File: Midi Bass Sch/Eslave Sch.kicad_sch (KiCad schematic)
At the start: 16 parts, among them M1 Stepper_Motor_bipolar, Q9 BDW93C, SW1 SW_Push, U2 PIC16F1788, U4 TMC2209

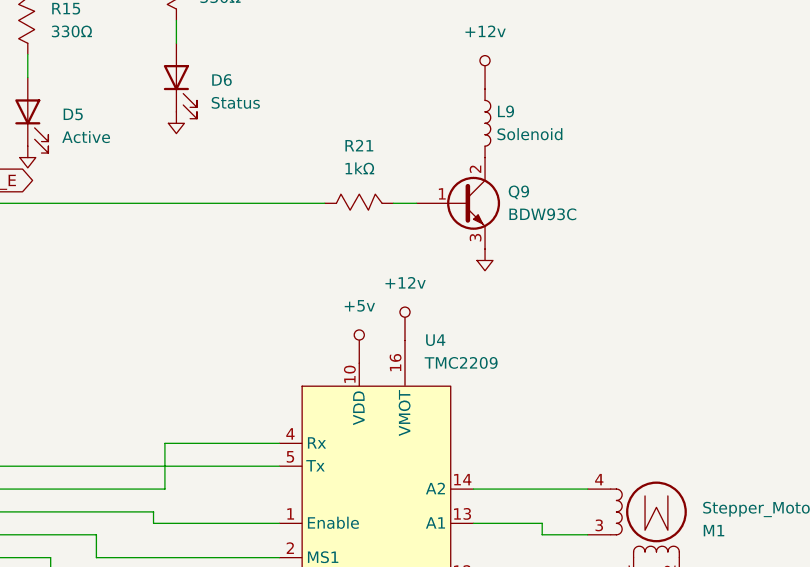
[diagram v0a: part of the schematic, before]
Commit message: updated stepper voltage
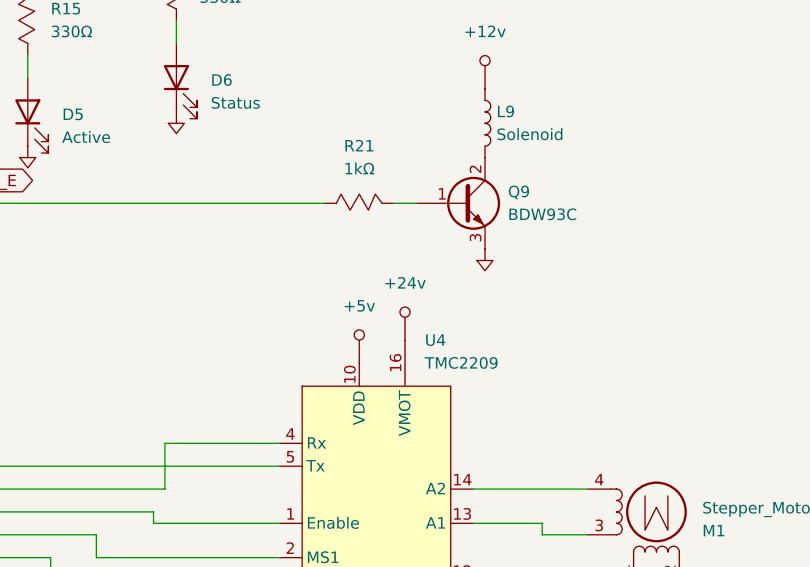
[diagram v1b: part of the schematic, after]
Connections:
- net +12v: no longer U4.16 (VMOT)
- new net +24v: U4.16 (VMOT)

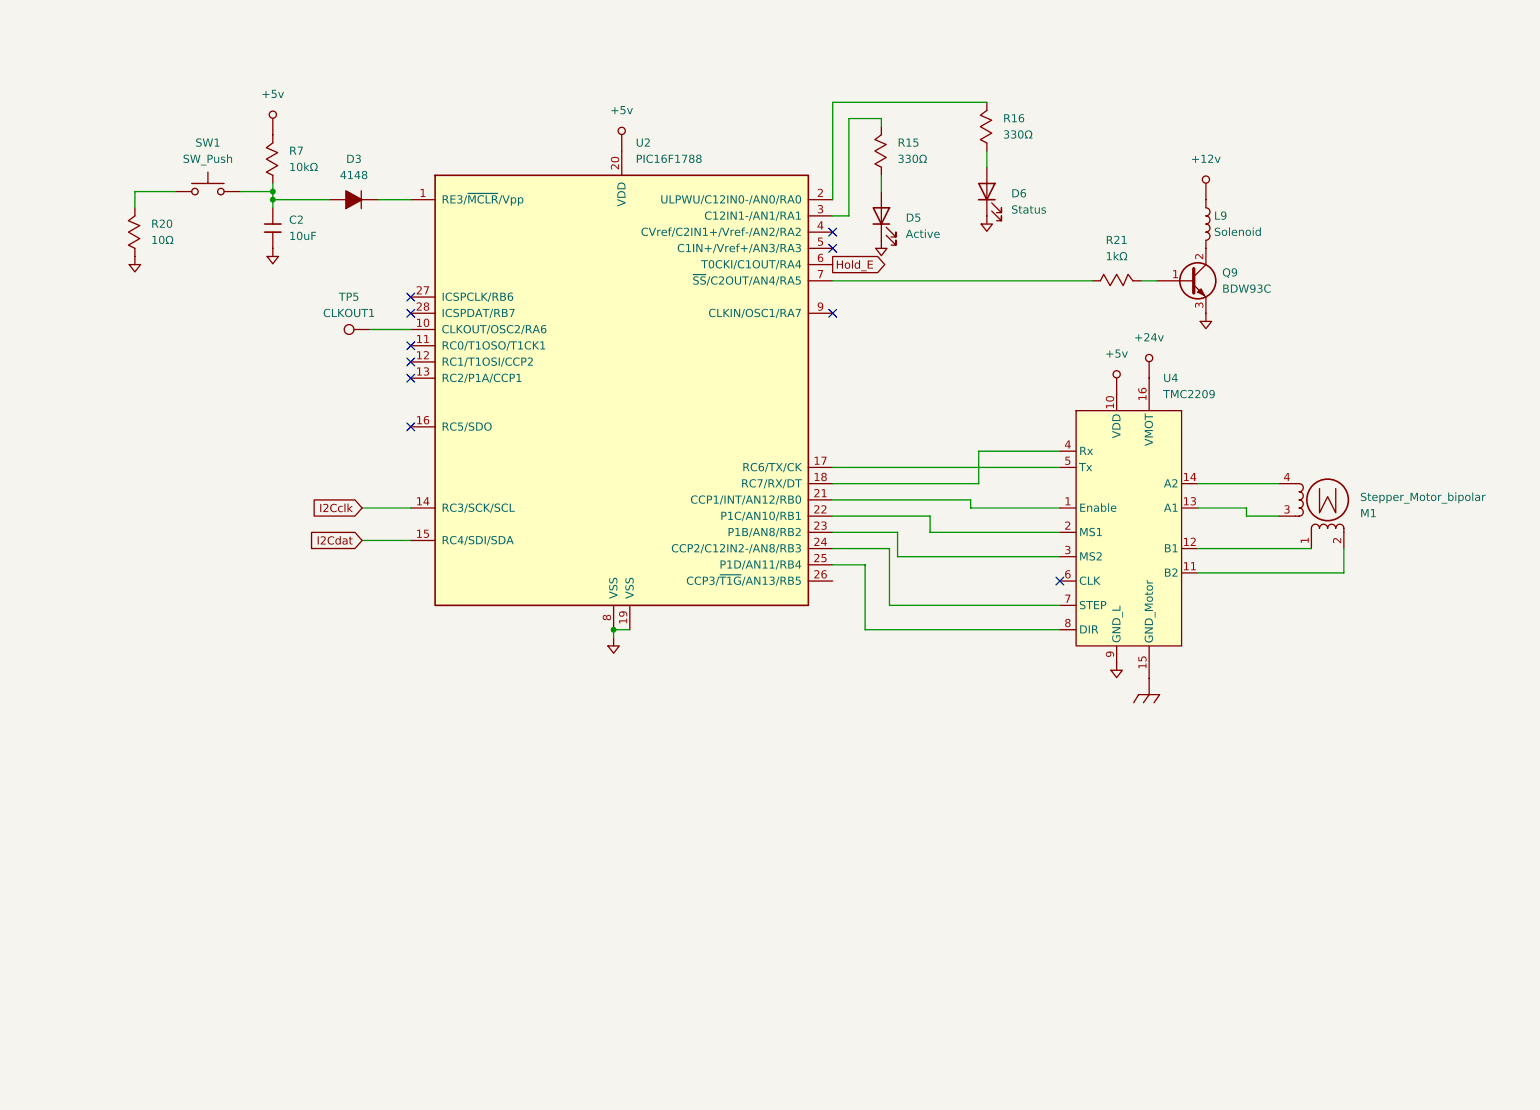
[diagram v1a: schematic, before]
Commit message: updated slave to 1789 to reflect new design updated 1789 to reflect thin flat pack
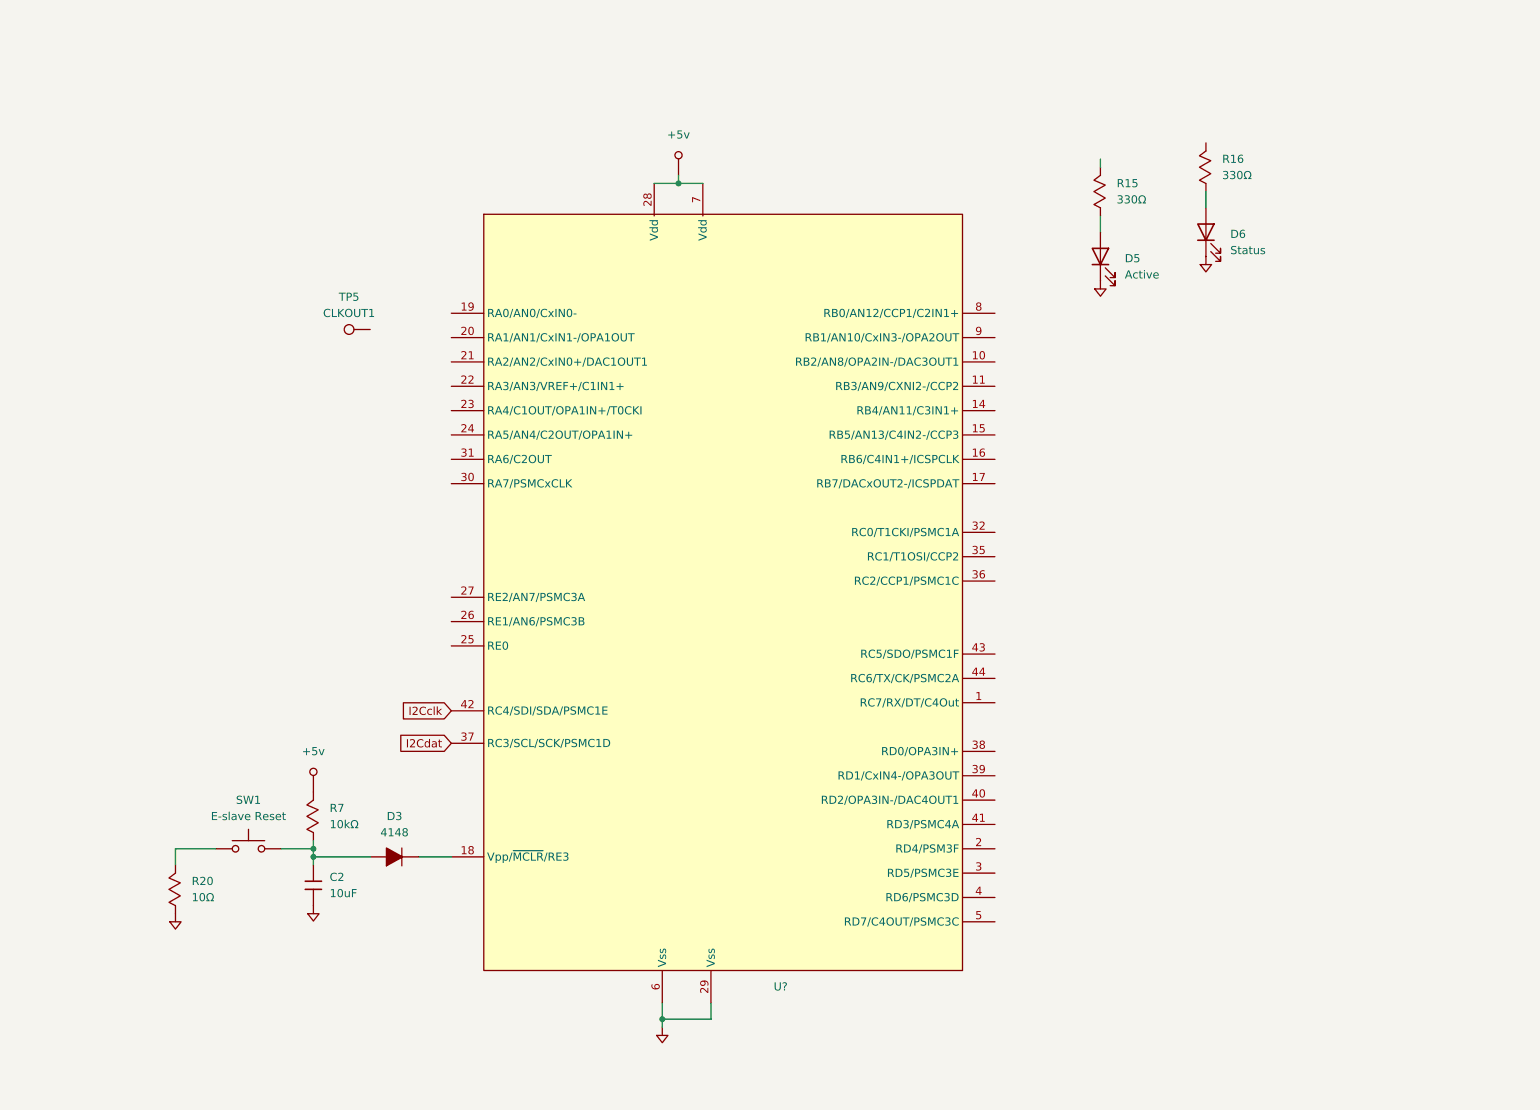
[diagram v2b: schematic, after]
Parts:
- removed L9: Solenoid, symbol Device:L
- removed M1: Stepper_Motor_bipolar, symbol Motor:Stepper_Motor_bipolar
- removed Q9: BDW93C, symbol Device:Q_NPN_BCE
- removed R21: 1kΩ, symbol Custom Symbols:Resistor_Mod
- removed U2: PIC16F1788, symbol Owen's Symbols:PIC16F1788_2
- removed U4: TMC2209, symbol Digital ICS:TMC2209
- added U?: ~, symbol Owen's Symbols:PIC16F1789_44
- SW1: value SW_Push -> E-slave Reset
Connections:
- net +5v: now also U?.28 (Vdd), U?.7 (Vdd)
- net GND: now also U?.29 (Vss), U?.6 (Vss)
- net at D3.2: now also U?.18 (Vpp/~{MCLR}/RE3)
- no-connect marks 10 -> 0
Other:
- moved on the sheet: C2, D3, D5, D6, R15, R16, R20, R7, SW1

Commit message: added flags to E-slave
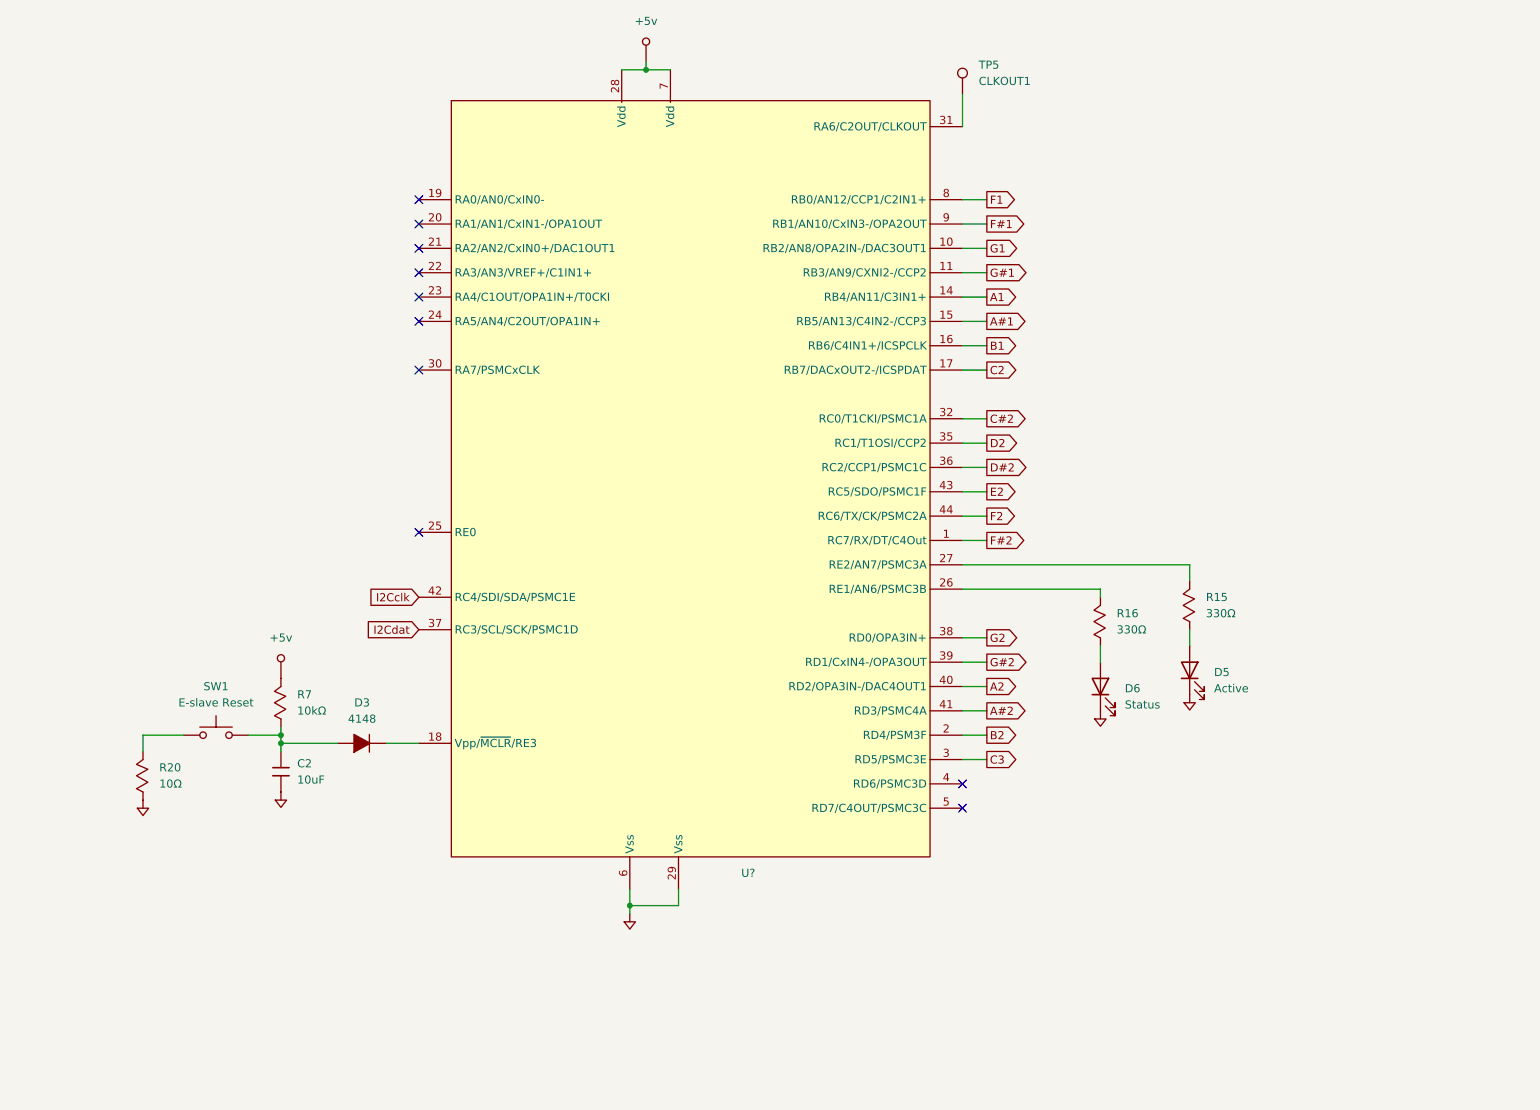
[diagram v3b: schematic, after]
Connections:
- net at TP5.1: now also U?.31 (RA6/C2OUT/CLKOUT)
- net at R16.2: now also U?.1 (RC7/RX/DT/C4Out)
- net G1: now reaches U?.10 (RB2/AN8/OPA2IN-/DAC3OUT1)
- net G#1: now reaches U?.11 (RB3/AN9/CXNI2-/CCP2)
- net A1: now reaches U?.14 (RB4/AN11/C3IN1+)
- net A#1: now reaches U?.15 (RB5/AN13/C4IN2-/CCP3)
- net B1: now reaches U?.16 (RB6/C4IN1+/ICSPCLK)
- net C2: now reaches U?.17 (RB7/DACxOUT2-/ICSPDAT)
- net B2: now reaches U?.2 (RD4/PSM3F)
- net C3: now reaches U?.3 (RD5/PSMC3E)
- net C#2: now reaches U?.32 (RC0/T1CKI/PSMC1A)
- net D2: now reaches U?.35 (RC1/T1OSI/CCP2)
- net D#2: now reaches U?.36 (RC2/CCP1/PSMC1C)
- net E2: now reaches U?.37 (RC3/SCL/SCK/PSMC1D)
- net G2: now reaches U?.38 (RD0/OPA3IN+)
- net G#2: now reaches U?.39 (RD1/CxIN4-/OPA3OUT)
- net A2: now reaches U?.40 (RD2/OPA3IN-/DAC4OUT1)
- net A#2: now reaches U?.41 (RD3/PSMC4A)
- net F2: now reaches U?.42 (RC4/SDI/SDA/PSMC1E)
- net F#2: now reaches U?.43 (RC5/SDO/PSMC1F)
- net at U?.44 (RC6/TX/CK/PSMC2A): now also R15.2
- net F1: now reaches U?.8 (RB0/AN12/CCP1/C2IN1+)
- net F#1: now reaches U?.9 (RB1/AN10/CxIN3-/OPA2OUT)
- no-connect marks 0 -> 10
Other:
- moved on the sheet: C2, D3, D5, D6, R15, R16, R20, R7, SW1, TP5, U?

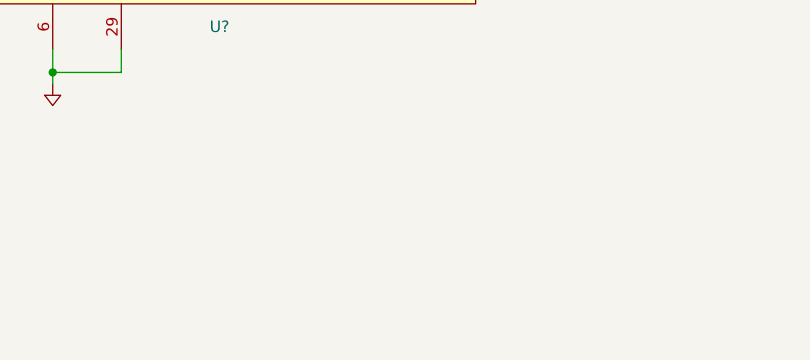
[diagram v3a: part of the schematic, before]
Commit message: added schematic page for solenoid array for E-slave
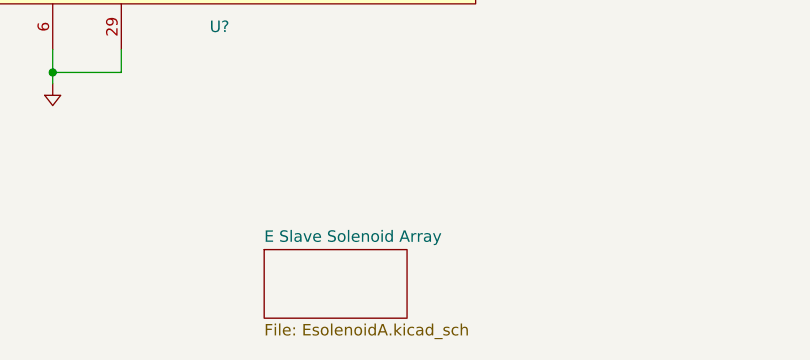
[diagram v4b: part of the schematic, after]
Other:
- added sheet E Slave Solenoid Array (EsolenoidA.kicad_sch)
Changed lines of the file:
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@@
+		)
+	)
+	(sheet
+		(at 137.795 177.165)
+		(size 15.875 7.62)
+		(fields_autoplaced yes)
+		(stroke
+			(width 0.1524)
+			(type solid)
+		)
+		(fill
+			(color 255 255 194 1.0000)
+		)
+		(property "Sheetname" "E Slave Solenoid Array"
+			(at 137.795 176.4534 0)
+			(effects
+				(font
+					(size 1.27 1.27)
+				)
+				(justify left bottom)
+			)
+		)
+		(property "Sheetfile" "EsolenoidA.kicad_sch"
+			(at 137.795 185.3696 0)
+			(effects
+				(font
+					(size 1.27 1.27)
+				)
+				(justify left top)
+			)
+		)
+		(instances
+			(project "Midi Bass Sch"
+				(path "/06818073-fb22-48ee-acc5-6dedd827034e/55f5fc9c-362b-429f-ad6f-f98ffe4c4860"
+					(page "9")
+				)
+			)
 		)
 	)

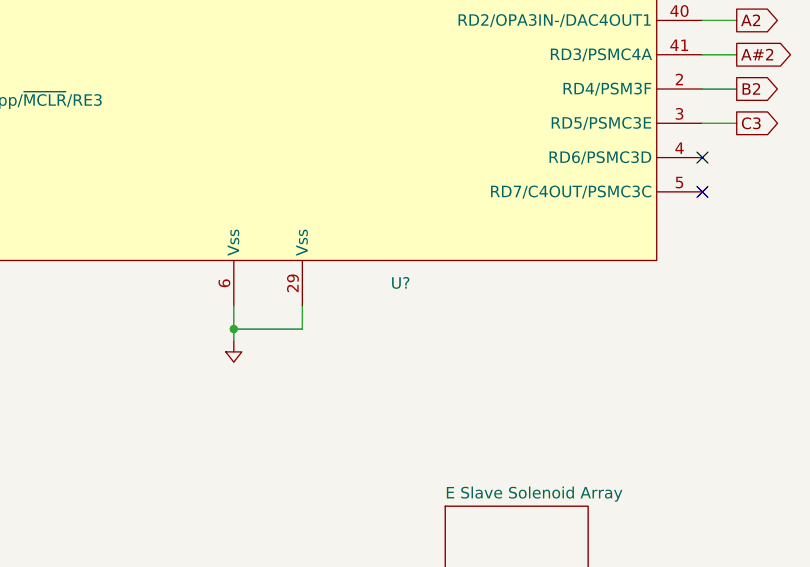
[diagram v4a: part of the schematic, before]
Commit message: updated schematic numbers
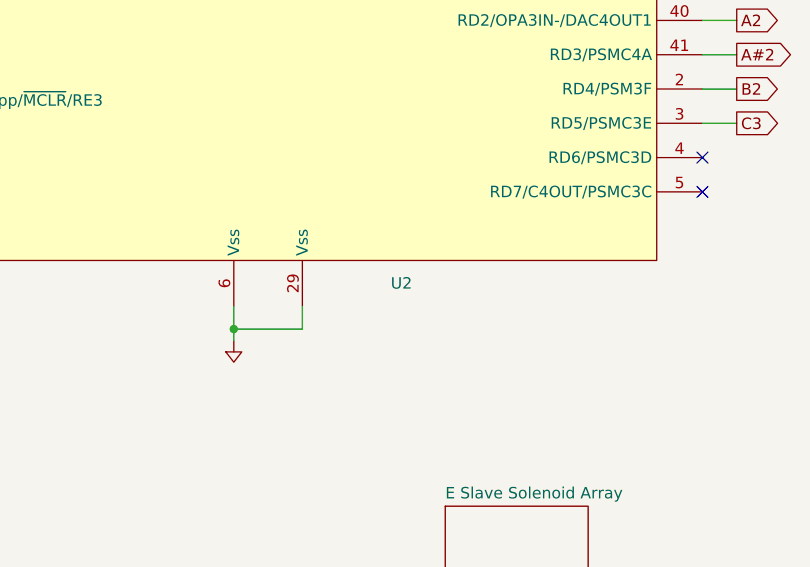
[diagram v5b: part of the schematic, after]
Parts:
- gave numbers to parts that had none: 1
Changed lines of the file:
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@@
 		(dnp no)
 		(fields_autoplaced yes)
-		(property "Reference" "U?"
+		(property "Reference" "U2"
 			(at 131.7341 152.4 0)
 			(effects
@@
 			(project ""
 				(path "/06818073-fb22-48ee-acc5-6dedd827034e/55f5fc9c-362b-429f-ad6f-f98ffe4c4860"
-					(reference "U?")
+					(reference "U2")
 					(unit 1)
 				)

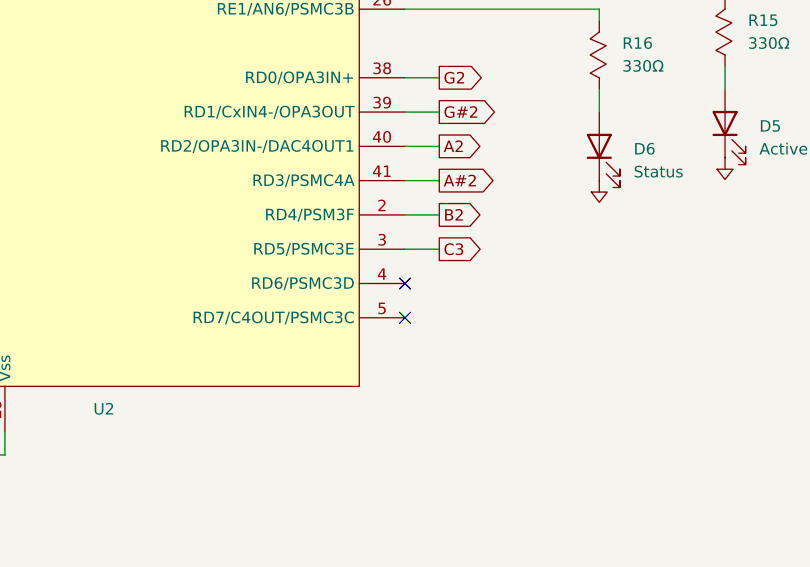
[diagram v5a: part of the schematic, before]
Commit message: added opto isolation to plucking solenoids
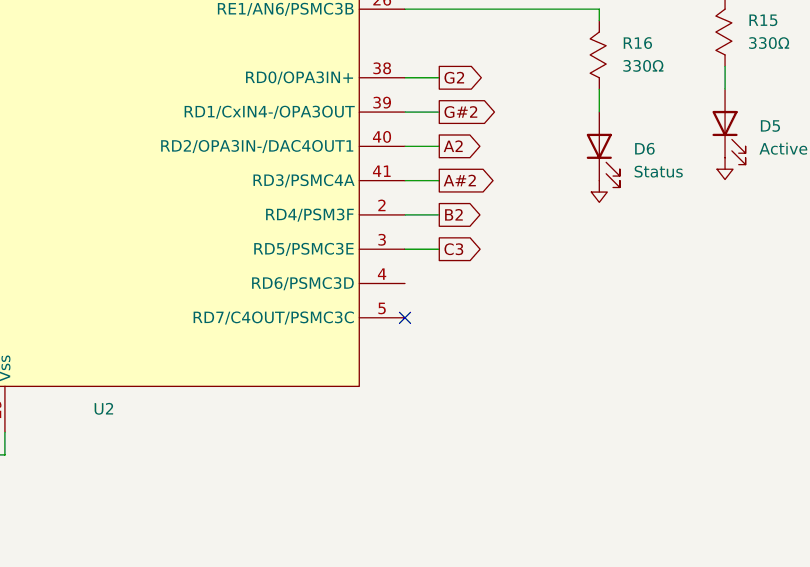
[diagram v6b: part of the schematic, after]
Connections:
- no-connect marks 10 -> 9
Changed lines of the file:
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@@
-	)
-	(no_connect
-		(at 166.37 138.43)
 	)
 	(no_connect
